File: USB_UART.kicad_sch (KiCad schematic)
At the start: 5 parts, among them J1 USB Type C Connector, U4 FT232RL

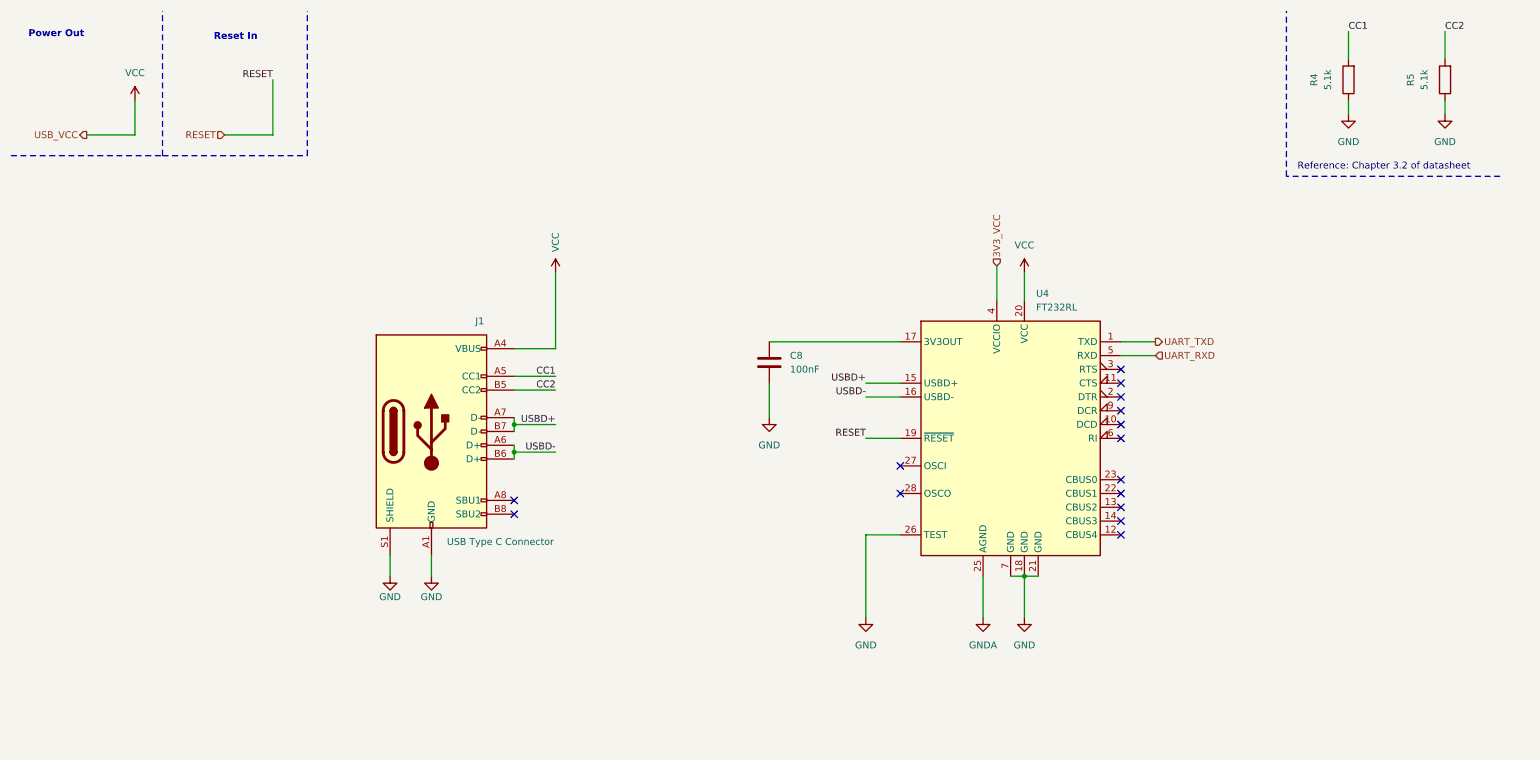
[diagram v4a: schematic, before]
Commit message: feat(LEDs): Added LEDs to the USB UART
Added a power LED and RX TX LEDs to the CBUS pins
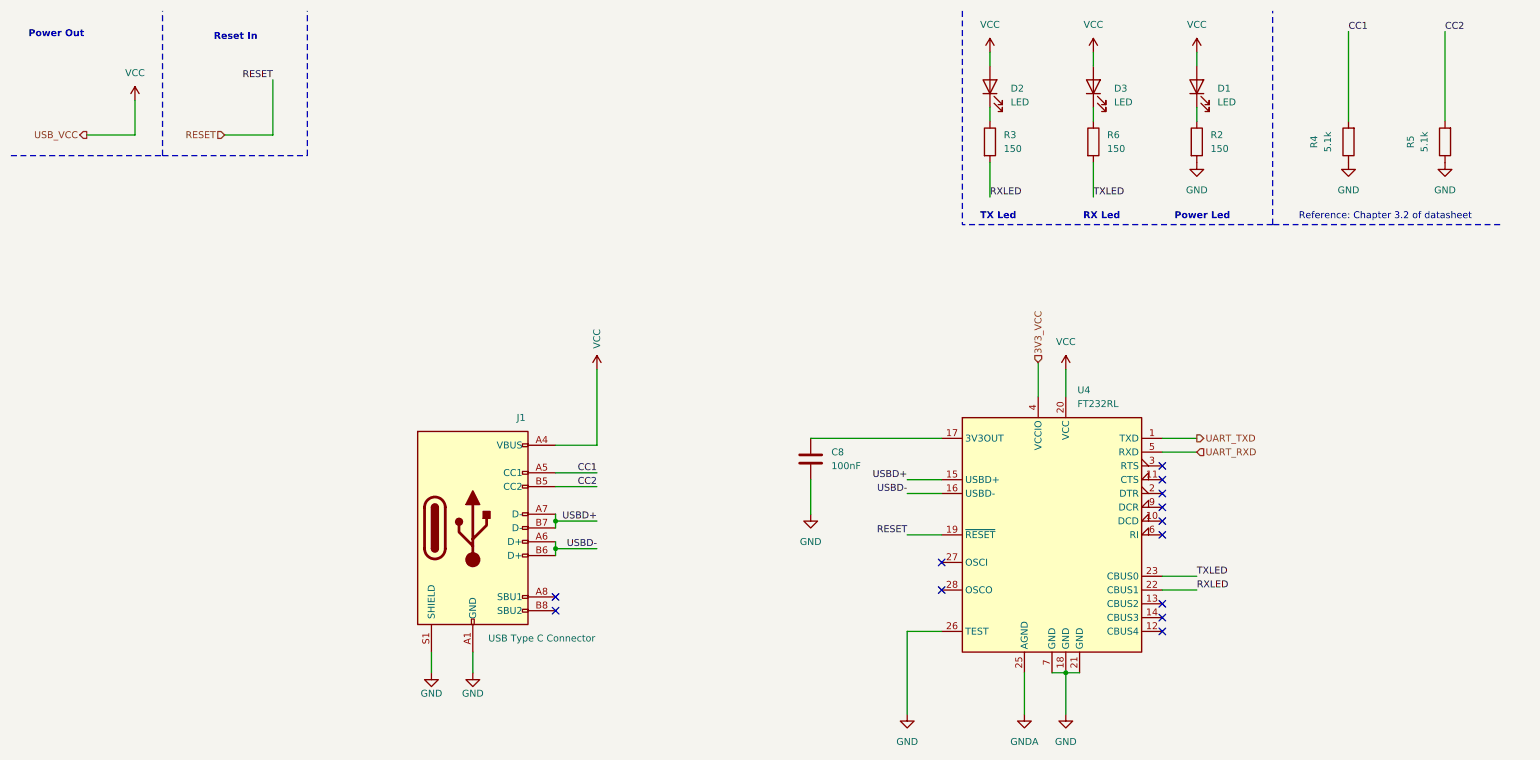
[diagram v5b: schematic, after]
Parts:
- added D1, D2, D3: LED, symbol Device:LED
- added R2, R3, R6: 150, symbol Device:R
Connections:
- net GND: now also R2.2
- net VCC: now also D1.2 (A), D2.2 (A), D3.2 (A)
- net RXLED: now reaches U4.22 (CBUS1)
- net RXLED: now also R3.2
- net TXLED: now reaches U4.23 (CBUS0)
- net TXLED: now also R6.2
- new net: D3.1 (K), R6.1
- new net: D1.1 (K), R2.1
- new net: D2.1 (K), R3.1
- no-connect marks 15 -> 13
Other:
- note added: "Power Led"
- note added: "RX Led"
- note added: "TX Led"
- moved on the sheet: C8, J1, R4, R5, U4

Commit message: feat(LED_Footprints): Added Footprints to the LEDs and its Resistors
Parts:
- D1, D2, D3: footprint (none) -> LED_SMD:LED_0603_1608Metric_Pad1.05x0.95mm_HandSolder
- R2, R3, R6: footprint (none) -> Resistor_SMD:R_0603_1608Metric_Pad0.98x0.95mm_HandSolder
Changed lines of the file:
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@@
 			)
 		)
-		(property "Footprint" ""
+		(property "Footprint" "LED_SMD:LED_0603_1608Metric_Pad1.05x0.95mm_HandSolder"
 			(at 209.55 26.67 0)
 			(effects
@@
 			)
 		)
-		(property "Footprint" ""
+		(property "Footprint" "Resistor_SMD:R_0603_1608Metric_Pad0.98x0.95mm_HandSolder"
 			(at 226.822 36.83 90)
 			(effects
@@
 			)
 		)
-		(property "Footprint" ""
+		(property "Footprint" "LED_SMD:LED_0603_1608Metric_Pad1.05x0.95mm_HandSolder"
 			(at 228.6 26.67 0)
 			(effects
@@
 			)
 		)
-		(property "Footprint" ""
+		(property "Footprint" "Resistor_SMD:R_0603_1608Metric_Pad0.98x0.95mm_HandSolder"
 			(at 188.722 36.83 90)
 			(effects
@@
 			)
 		)
-		(property "Footprint" ""
+		(property "Footprint" "Resistor_SMD:R_0603_1608Metric_Pad0.98x0.95mm_HandSolder"
 			(at 207.772 36.83 90)
 			(effects
@@
 			)
 		)
-		(property "Footprint" ""
+		(property "Footprint" "LED_SMD:LED_0603_1608Metric_Pad1.05x0.95mm_HandSolder"
 			(at 190.5 26.67 0)
 			(effects
